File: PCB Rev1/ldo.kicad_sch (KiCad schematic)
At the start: 4 parts, among them U5 TPS7A4700RGWR

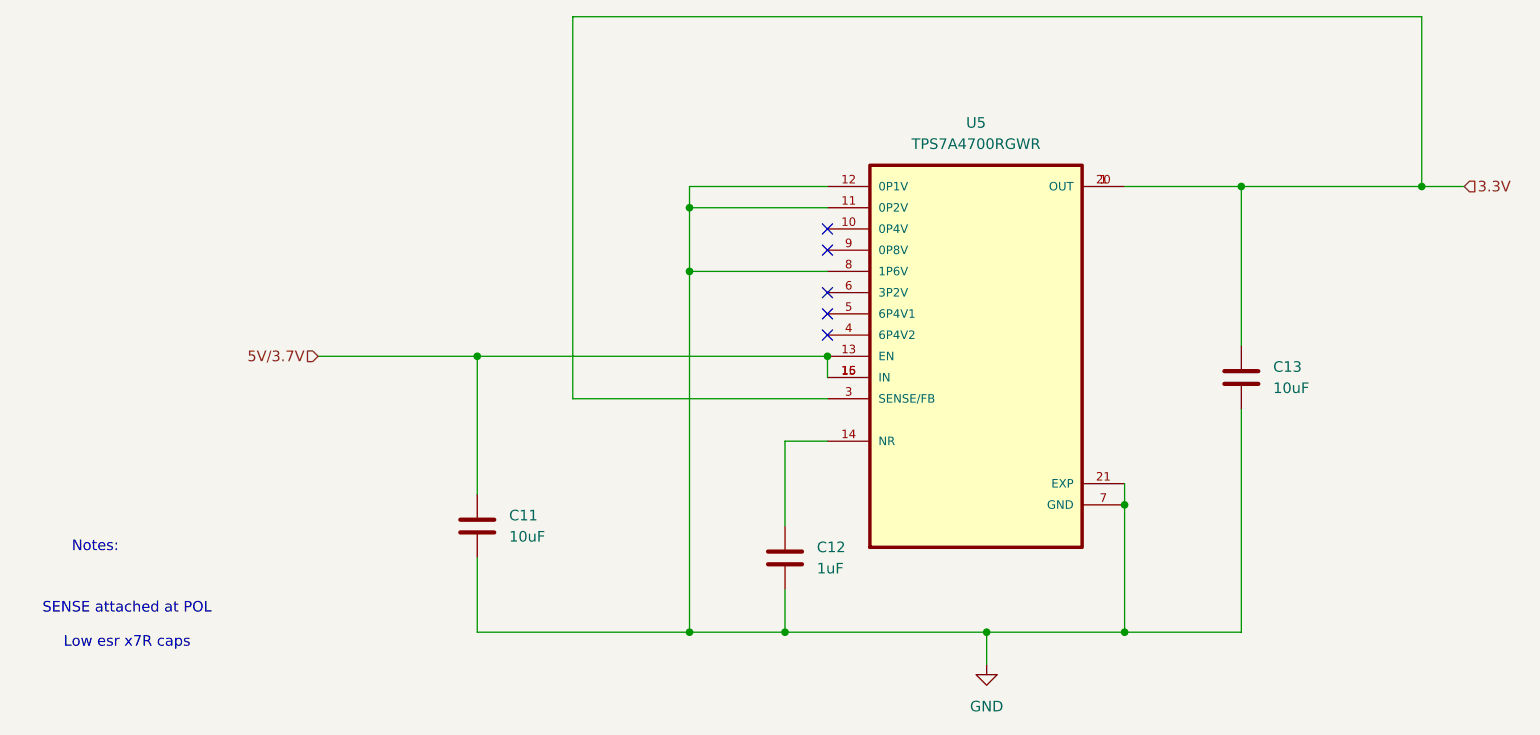
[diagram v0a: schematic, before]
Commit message: rev 2 schematic with minor changes, final send out before layout
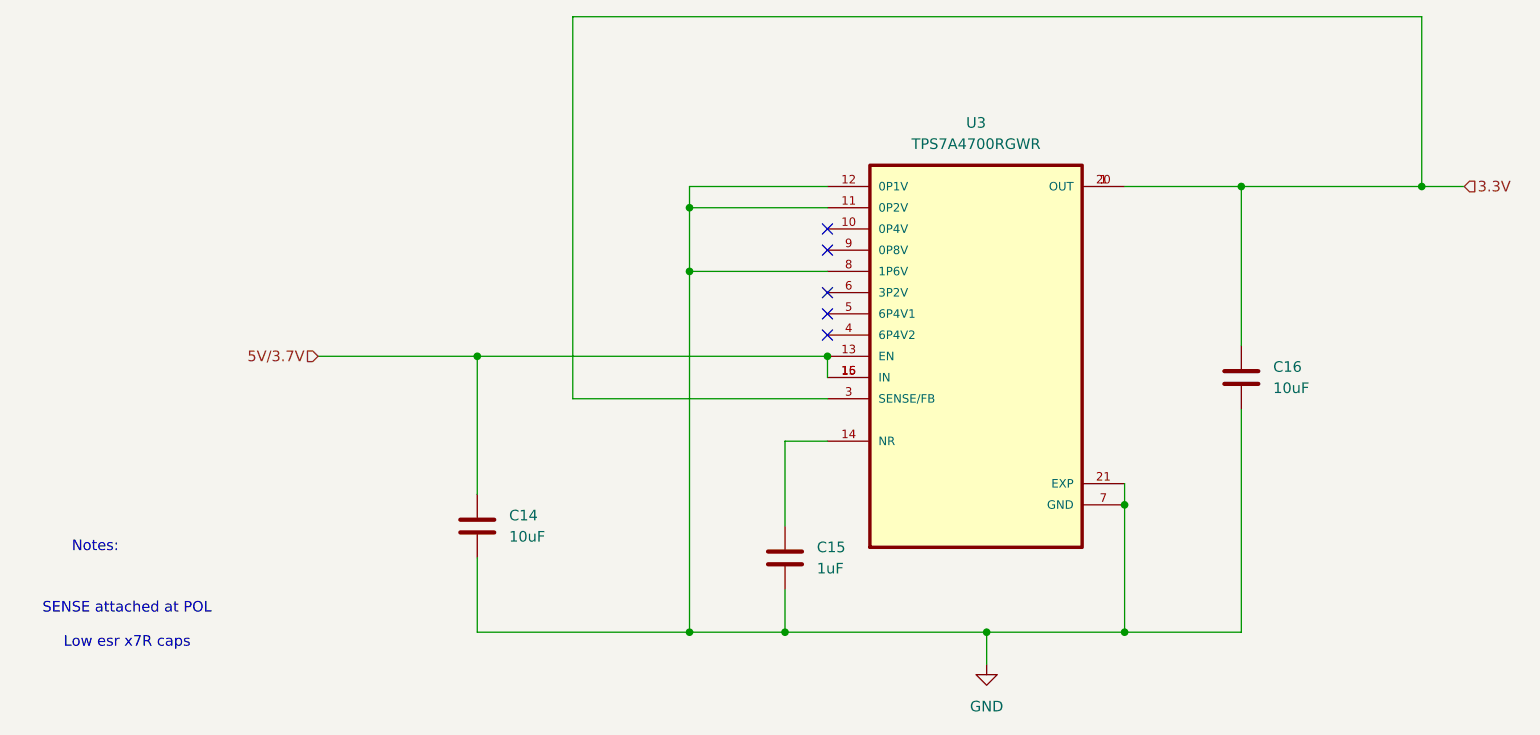
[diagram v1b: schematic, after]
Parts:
- renumbered C11 to C14, C12 to C15, C13 to C16, U5 to U3
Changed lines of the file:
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@@
 		(dnp no)
 		(fields_autoplaced yes)
-		(property "Reference" "C12"
+		(property "Reference" "C15"
 			(at 125.73 125.7299 0)
 			(effects
@@
 			(project ""
 				(path "/adf54578-0edd-4ea8-a516-35041fcd2885/d189fb14-1a29-4323-9eac-9960cf5e0868"
-					(reference "C12")
+					(reference "C15")
 					(unit 1)
 				)
@@
 		(dnp no)
 		(fields_autoplaced yes)
-		(property "Reference" "C13"
+		(property "Reference" "C16"
 			(at 180.34 104.1399 0)
 			(effects
@@
 			(project ""
 				(path "/adf54578-0edd-4ea8-a516-35041fcd2885/d189fb14-1a29-4323-9eac-9960cf5e0868"
-					(reference "C13")
+					(reference "C16")
 					(unit 1)
 				)
@@
 		(dnp no)
 		(fields_autoplaced yes)
-		(property "Reference" "#PWR019"
+		(property "Reference" "#PWR016"
 			(at 146.05 146.05 0)
 			(effects
@@
 			(project ""
 				(path "/adf54578-0edd-4ea8-a516-35041fcd2885/d189fb14-1a29-4323-9eac-9960cf5e0868"
-					(reference "#PWR019")
+					(reference "#PWR016")
 					(unit 1)
 				)
@@
 		(dnp no)
 		(fields_autoplaced yes)
-		(property "Reference" "C11"
+		(property "Reference" "C14"
 			(at 88.9 121.9199 0)
 			(effects
@@
 			(project ""
 				(path "/adf54578-0edd-4ea8-a516-35041fcd2885/d189fb14-1a29-4323-9eac-9960cf5e0868"
-					(reference "C11")
+					(reference "C14")
 					(unit 1)
 				)
@@
 		(dnp no)
 		(fields_autoplaced yes)
-		(property "Reference" "U5"
+		(property "Reference" "U3"
 			(at 144.78 74.93 0)
 			(effects
@@
 			(project ""
 				(path "/adf54578-0edd-4ea8-a516-35041fcd2885/d189fb14-1a29-4323-9eac-9960cf5e0868"
-					(reference "U5")
+					(reference "U3")
 					(unit 1)
 				)
